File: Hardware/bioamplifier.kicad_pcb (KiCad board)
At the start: 4 copper layers, 71.8 x 40.5 mm, 94 parts, among them J1 Conn_01x07_Socket, J2 Conn_01x26_Pin, J3 Conn_01x07_Socket, J4 Jumper, J5 Jumper, U1 ADS1299IPAG, U10 TPD4E1B06DCKR, U11 LM2665M6, U2 TPD4E1B06DCKR, U3 TPD4E1B06DCKR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

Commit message: TODO: GND pours & planes separation
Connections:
- C11 pad 1: GNDA -> AVSS
- C12 pad 1: GNDA -> AVSS
- C13 pad 1: GNDA -> AVSS
- C14 pad 1: GNDA -> AVSS
- C15 pad 1: GNDA -> AVSS
- C16 pad 1: GNDA -> AVSS
- C17 pad 1: GNDA -> AVSS
- C18 pad 1: GNDA -> AVSS
- C25 pad 1: GNDA -> AVSS
- C26 pad 1: GNDA -> AVSS
- C28 pad 1: GNDA -> AVSS
- C31 pad 1: GNDA -> AVSS
- C32 pad 1: GNDA -> AVSS
- C33 pad 1: GNDA -> AVSS
- C34 pad 1: GNDA -> AVSS
- C35 pad 1: GNDA -> AVSS
- C36 pad 1: GNDA -> AVSS
- C37 pad 2: GNDA -> AVSS
- C38 pad 1: GNDA -> AVSS
- C39 pad 1: GNDA -> AVSS
- C40 pad 2: GNDA -> AVSS
- C42 pad 2: GNDA -> AVSS
- C43 pad 2: GNDA -> AVSS
- C44 pad 2: GNDA -> AVSS
- C46 pad 2: GNDA -> AVSS
- J2 pad 1: GNDA -> AVSS
- J2 pad 2: GNDA -> AVSS
- J2 pad 23: /Electrodes input/AGND -> AVSS
- J2 pad 24: /Electrodes input/AGND -> AVSS
- J2 pad 25: /Electrodes input/AVDD_ED -> AVDD
- J2 pad 26: /Electrodes input/AVDD_ED -> AVDD
- J4 pad 1: GNDA -> AVSS
- R15 pad 2: GNDA -> AVSS
- U1 pad 31: GNDA -> AVSS
- U1 pad 60: GNDA -> AVSS
- U10 pad 3: GNDA -> AVSS
- U11 pad 2: GNDA -> AVSS
- U2 pad 3: GNDA -> AVSS
- U3 pad 3: GNDA -> AVSS
- U4 pad 3: GNDA -> AVSS
- U5 pad 2: /Electrodes input/AVDD_ED -> AVDD
- U5 pad 3: GNDA -> AVSS
- U7 pad 1: GNDA -> AVSS
- U8 pad 2: GNDA -> AVSS
- U8 pad 4: GNDA -> AVSS
- U9 pad 3: GNDA -> AVSS
- U9 pad 4: GNDA -> AVSS
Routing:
- net AVDD: track 68.2 -> 102.1 mm, vias 2 -> 3
- net GNDA: track 32.9 -> 0.00 mm, vias 6 -> 0
- net AVSS: track 93.0 -> 125.9 mm, vias 5 -> 11
- net /Electrodes input/AVDD_ED: track 8.20 -> 0.00 mm
- added copper zone on F.Cu, net AVSS
- added copper zone on In2.Cu, net AVSS
- removed copper zone on B.Cu, net GNDA
- removed copper zone on F.Cu, net GNDA
- removed copper zone on In2.Cu, net GNDA

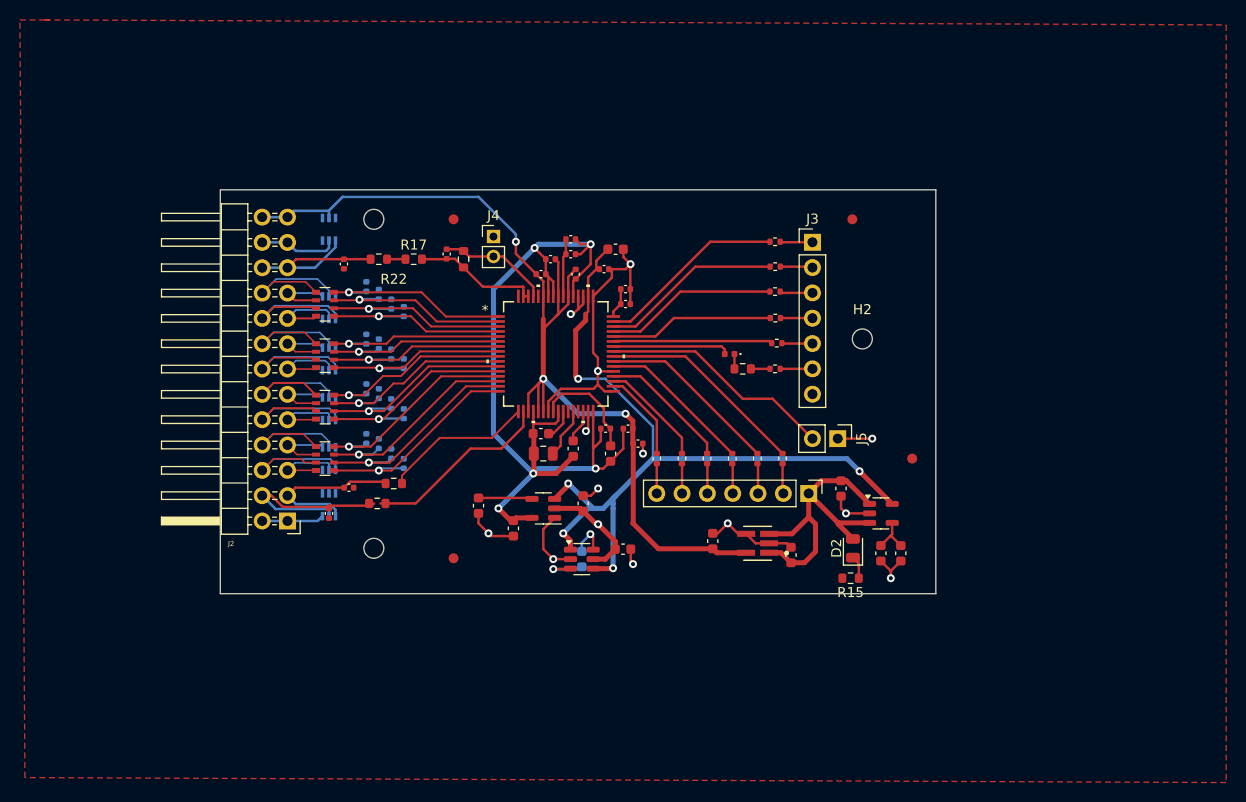
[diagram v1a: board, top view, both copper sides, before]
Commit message: Fix GndA Avss connection, standardize grids
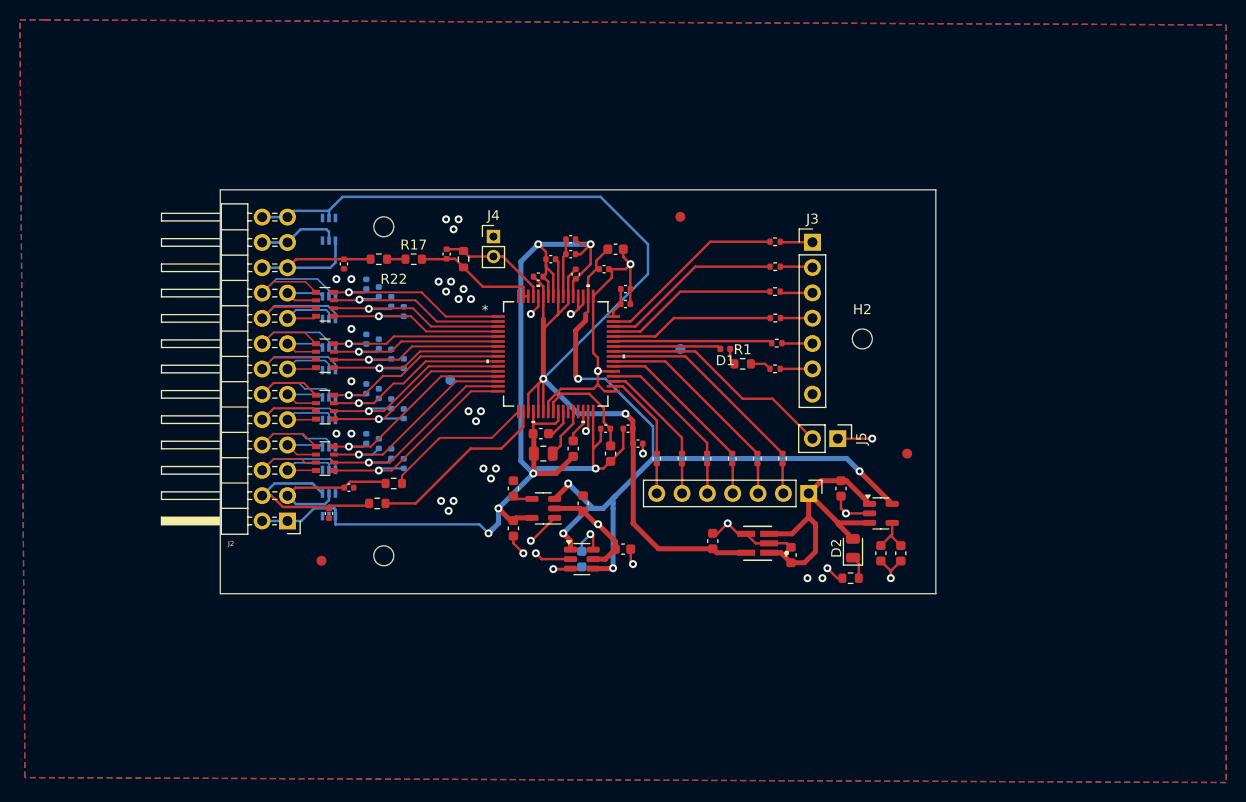
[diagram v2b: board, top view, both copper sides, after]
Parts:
- added FID5: Fiducial, Fiducial:Fiducial_1mm_Mask3mm, B.Cu at (73.7, 91.1)
- FID1: moved to B.Cu
- moved FID3 22.8 mm to (96.8, 74.8)
- moved FID1 21.6 mm to (96.8, 88.0)
- moved FID4 13.3 mm to (60.8, 109.2)
- moved C44 3.90 mm to (80.0, 102.0), turned to 90 degrees
- moved H1 1.25 mm to (67.0, 75.8)
- moved H3 1.25 mm to (67.0, 108.8)
- moved FID2 0.71 mm to (119.5, 98.5)
- moved D1 0.67 mm to (101.2, 88.0)
- moved R1 0.50 mm to (103.0, 89.5)
- moved C22 0.37 mm to (82.5, 80.8)
- moved C18 0.25 mm to (67.8, 83.2)
- moved C32 0.25 mm to (66.5, 82.3)
- moved C33 0.25 mm to (65.2, 81.5)
- turned C24 to 180 degrees
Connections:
- C11 pad 1: AVSS -> GNDA
- C12 pad 1: AVSS -> GNDA
- C13 pad 1: AVSS -> GNDA
- C14 pad 1: AVSS -> GNDA
- C15 pad 1: AVSS -> GNDA
- C16 pad 1: AVSS -> GNDA
- C17 pad 1: AVSS -> GNDA
- C18 pad 1: AVSS -> GNDA
- C24 pad 1: AVSS -> AVDD
- C24 pad 2: AVDD -> AVSS
- C25 pad 1: AVSS -> GNDA
- C26 pad 1: AVSS -> GNDA
- C28 pad 1: AVSS -> GNDA
- C31 pad 1: AVSS -> GNDA
- C32 pad 1: AVSS -> GNDA
- C33 pad 1: AVSS -> GNDA
- C34 pad 1: AVSS -> GNDA
- C35 pad 1: AVSS -> GNDA
- C36 pad 1: AVSS -> GNDA
- C37 pad 2: AVSS -> GNDA
- C38 pad 1: AVSS -> GNDA
- C39 pad 1: AVSS -> GNDA
- C40 pad 2: AVSS -> GNDA
- C42 pad 2: AVSS -> GNDA
- C43 pad 2: AVSS -> GNDA
- C44 pad 2: AVSS -> GNDA
- C46 pad 2: AVSS -> GNDA
- J2 pad 23: AVSS -> GNDA
- J2 pad 24: AVSS -> GNDA
- J4 pad 1: AVSS -> GNDA
- R15 pad 2: AVSS -> GNDA
- U1 pad 31: AVSS -> GNDA
- U1 pad 60: AVSS -> GNDA
- U10 pad 3: AVSS -> GNDA
- U11 pad 2: AVSS -> GNDA
- U2 pad 3: AVSS -> GNDA
- U3 pad 3: AVSS -> GNDA
- U4 pad 3: AVSS -> GNDA
- U5 pad 3: AVSS -> GNDA
- U5 pad 5: /Electrodes input/AGND -> GNDA
- U7 pad 1: AVSS -> GNDA
- U8 pad 2: AVSS -> GNDA
- U8 pad 4: AVSS -> GNDA
- U9 pad 1: /Electrodes input/REF1 -> AVSS
- U9 pad 2: /Electrodes input/REF2 -> unconnected-(U9-IO2-Pad2)
- U9 pad 3: AVSS -> GNDA
- U9 pad 4: AVSS -> /Electrodes input/REF2
- U9 pad 5: unconnected-(U9-IO4-Pad5) -> /Electrodes input/REF1
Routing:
- net GNDA: track 0.00 -> 34.5 mm, vias 0 -> 34
- net AVDD: track 102.1 -> 128.7 mm, vias 3 -> 2
- net /Electrodes input/AGND: track 7.92 -> 0.00 mm
- net AVSS: track 125.9 -> 120.5 mm, vias 11 -> 6
- net Net-(U7-NR): track 5.40 -> 1.98 mm
- net /Electrodes input/REF2: track 19.8 -> 18.5 mm
- net Net-(D1-A): track 11.8 -> 10.8 mm
- net /Electrodes input/BIAS: track 17.6 -> 18.5 mm
- net IN7N: track 19.8 -> 20.6 mm
- net SRB2: track 19.0 -> 18.5 mm
- added copper zone on B.Cu, net GNDA
- added copper zone on F.Cu, net GNDA
- removed copper zone on F.Cu, net AVSS
- removed copper zone on In2.Cu, net AVSS

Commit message: Flip capacitors from back
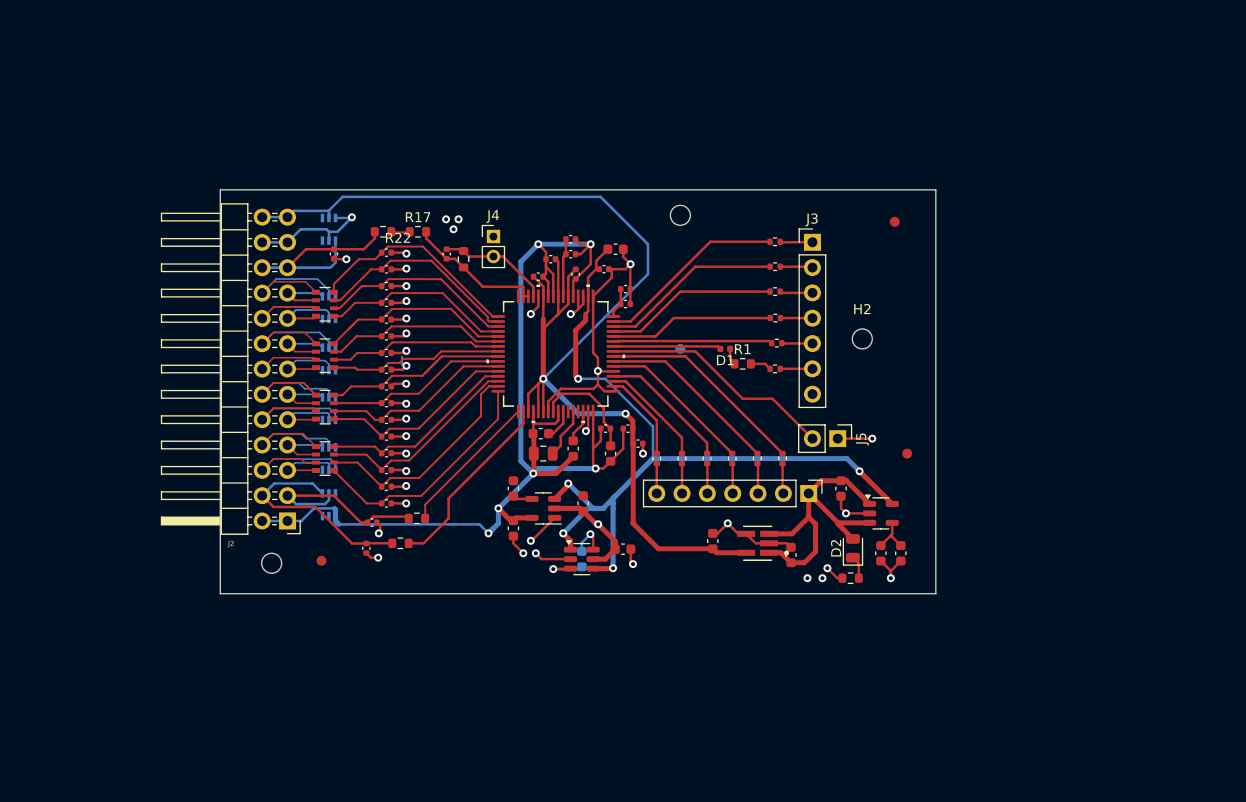
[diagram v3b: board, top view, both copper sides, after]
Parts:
- removed FID5: Fiducial, Fiducial:Fiducial_1mm_Mask3mm
- C11, C12, C13, C14, C15, C16, C17, C18, C26, C28, C31, C32, C33, C34, C35, C36: moved to F.Cu
- moved H1 29.8 mm to (96.8, 74.6)
- moved FID3 21.5 mm to (118.2, 75.2)
- moved H3 11.3 mm to (55.8, 109.5)
- moved C37 5.13 mm to (65.2, 108.0)
- moved R2 4.63 mm to (68.7, 107.5)
- moved C11 4.36 mm to (67.3, 103.5), turned to 180 degrees
- moved C38 4.20 mm to (65.8, 105.4)
- moved R20 4.20 mm to (70.3, 105.0)
- moved C33 3.75 mm to (67.3, 78.3), turned to 180 degrees
- moved C12 3.36 mm to (67.3, 101.8), turned to 180 degrees
- moved C13 2.87 mm to (67.3, 96.8), turned to 180 degrees
- moved C31 2.82 mm to (67.3, 85.1), turned to 180 degrees
- moved R17 2.78 mm to (70.4, 76.2)
- moved R22 2.78 mm to (66.9, 76.2)
- moved C26 2.76 mm to (67.3, 100.1), turned to 180 degrees
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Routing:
- net GNDA: track 34.5 -> 68.8 mm, vias 34 -> 33
- net /Electrodes input/N5: track 14.7 -> 5.95 mm
- net /Electrodes input/N7: track 14.7 -> 5.93 mm
- net /Electrodes input/REF2: track 18.5 -> 21.9 mm
- net /Electrodes input/REF1: track 16.2 -> 19.1 mm
- net IN5P: track 19.7 -> 17.3 mm, vias 1 -> 0
- net IN8N: track 19.5 -> 21.8 mm, vias 1 -> 0
- net IN4P: track 20.4 -> 18.2 mm, vias 1 -> 0
- net IN5N: track 19.3 -> 17.4 mm, vias 1 -> 0
- net /Electrodes input/BIAS: track 18.5 -> 20.4 mm
- net IN1P: track 22.4 -> 24.1 mm, vias 1 -> 0
- net IN3N: track 20.7 -> 19.1 mm, vias 1 -> 0
- net IN2N: track 21.3 -> 19.9 mm, vias 1 -> 0
- net IN8P: track 19.5 -> 20.8 mm, vias 1 -> 0
- net IN6N: track 18.5 -> 19.8 mm, vias 1 -> 0
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- removed copper zone on B.Cu, net GNDA
- removed copper zone on F.Cu, net GNDA
- removed copper zone on In1.Cu, net GNDD

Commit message: Feat: fix small connection error, made board bigger
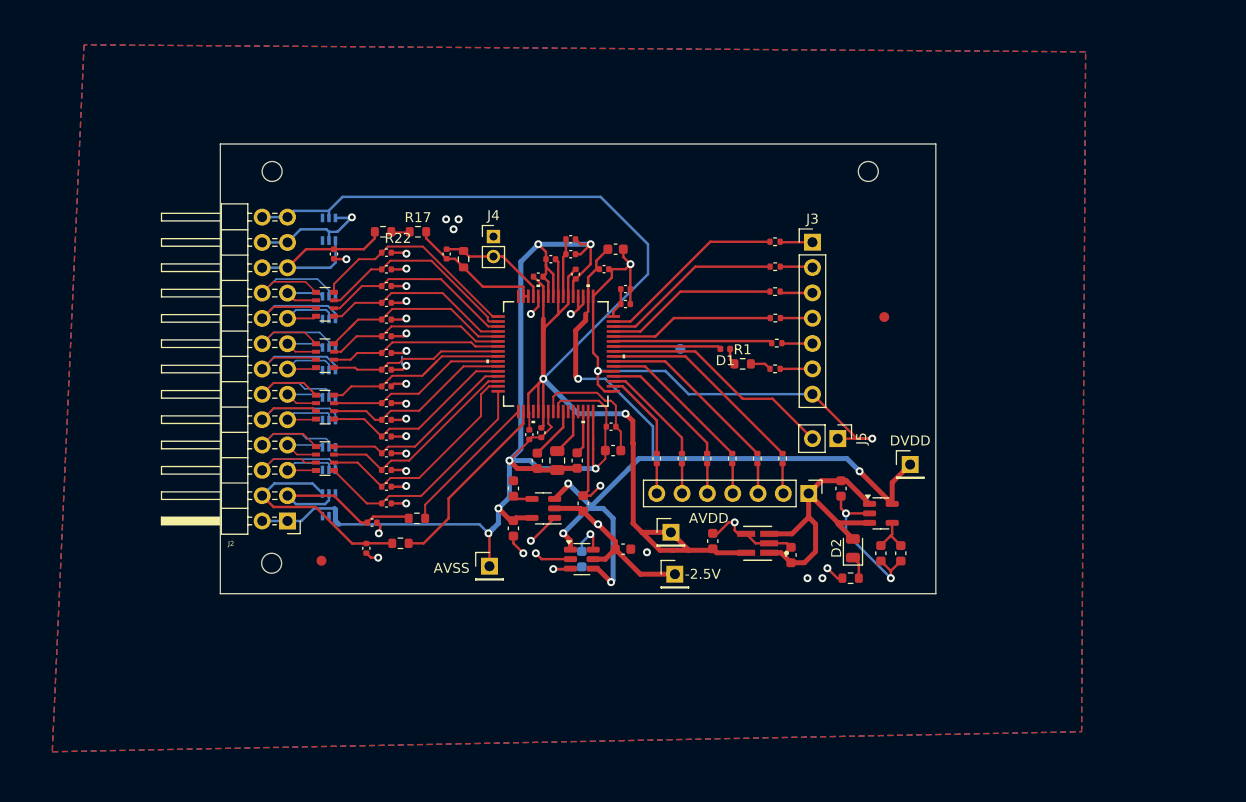
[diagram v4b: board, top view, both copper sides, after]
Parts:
- removed FID2: Fiducial, Fiducial:Fiducial_1mm_Mask3mm
- added -2.5V: -2.5v_test, Connector_PinHeader_2.54mm:PinHeader_1x01_P2.54mm_Vertical, F.Cu at (96.2, 110.6)
- added AVDD: 2.5v_reg_test, Connector_PinHeader_2.54mm:PinHeader_1x01_P2.54mm_Vertical, F.Cu at (95.8, 106.4)
- added AVSS: -2.5v_reg_test, Connector_PinHeader_2.54mm:PinHeader_1x01_P2.54mm_Vertical, F.Cu at (77.6, 109.8)
- added DVDD: dvdd_test, Connector_PinHeader_2.54mm:PinHeader_1x01_P2.54mm_Vertical, F.Cu at (119.8, 99.6)
- H1: moved to B.Cu
- moved H1 41.2 mm to (55.8, 70.2)
- moved H2 16.8 mm to (115.6, 70.2)
- moved C21 9.92 mm to (81.6, 96.6), turned to -90 degrees
- moved C1 9.76 mm to (82.8, 96.4), turned to -90 degrees
- moved FID3 9.61 mm to (117.2, 84.8)
- moved C10 2.75 mm to (82.4, 99.2), turned to -90 degrees
- moved C9 1.57 mm to (84.4, 99.2), turned to -90 degrees
- moved C8 1.26 mm to (86.4, 99.2)
- moved C4 0.59 mm to (89.8, 95.8)
- moved C5 0.39 mm to (90.0, 98.2), turned to 180 degrees
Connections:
- C1 pad 2: GNDD -> AVSS
- U1 pad 23: GNDD -> AVSS
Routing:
- net GNDD: track 46.6 -> 77.6 mm, vias 7 -> 6
- net AVSS: track 121.1 -> 130.7 mm
- net AVDD: track 128.7 -> 137.8 mm
- net /Electrodes input/N7: track 5.93 -> 14.7 mm
- net /Electrodes input/N5: track 5.95 -> 14.6 mm
- net GNDA: track 68.8 -> 76.5 mm
- net DVDD: track 83.3 -> 90.6 mm
- net -2.5V_UNREG: track 10.9 -> 17.9 mm
- net Net-(U1-VREFP): track 11.0 -> 13.2 mm
- net Net-(U1-VCAP4): track 3.10 -> 5.25 mm
- net Net-(U1-VCAP2): track 3.36 -> 4.40 mm
- added copper zone on B.Cu, net GNDA
- added copper zone on F.Cu, net GNDA
- added copper zone on In1.Cu, net GNDA
- added copper zone on In2.Cu, net GNDD
- removed copper zone on In2.Cu, net DVDD
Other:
- board size 71.8 x 40.5 mm -> 71.8 x 45.1 mm

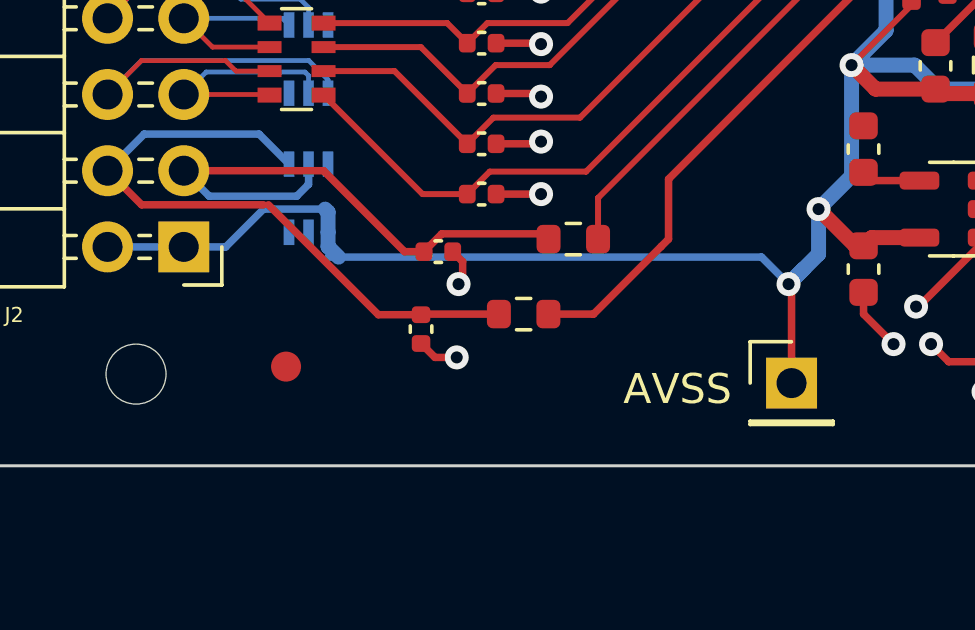
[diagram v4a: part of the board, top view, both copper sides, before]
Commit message: feat: fix AVSS electrode connection
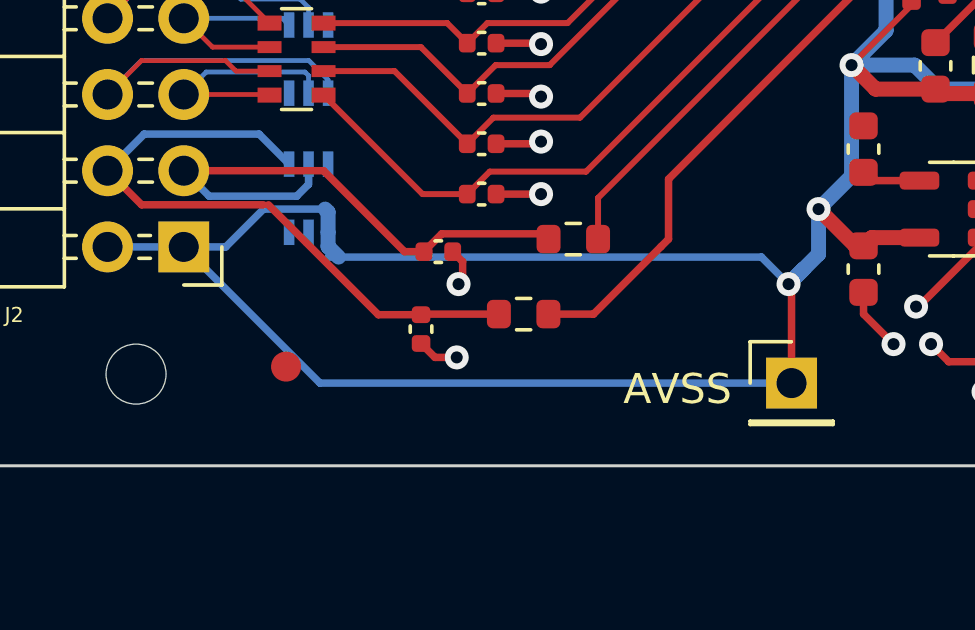
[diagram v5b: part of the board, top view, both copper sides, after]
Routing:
- net AVSS: track 130.7 -> 152.8 mm
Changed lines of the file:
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@@
+	)
+	(segment
+		(start 57.34 105.26)
+		(end 61.88 109.8)
+		(width 0.25)
+		(layer "B.Cu")
+		(net 28)
 	)
 	(segment
@@
 		(layer "B.Cu")
 		(net 28)
+	)
+	(segment
+		(start 61.88 109.8)
+		(end 77.6 109.8)
+		(width 0.25)
+		(layer "B.Cu")
+		(net 28)
